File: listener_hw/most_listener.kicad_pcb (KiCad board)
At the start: 2 copper layers, 130 x 90 mm, 125 parts, among them J1 1-1394640-1, J2 ANALYSER, J3 I2S, J4 VBAT_IN, J5 PLR135/T10, J6 PLT133/T10W, J7 RCA 75R, M1 Tang Nano 20K, M2 ESP32-DevKitC-VIE, U1 74LVC1G34, U10 TPS2553DBVR, U11 74LVC1G123, U12 DIR9001, U13 SRC4192, U14 LP5907MFX-3.3, U2 74LVC1G157, U3 74LVC1G125, U4 74LVC1G123, U5 TPS7B8133DRV, U6 LMR38020F, U7 Si514, U8 LP5907MFX-3.3, U9 74LVC1G79, X1 24.576MHz

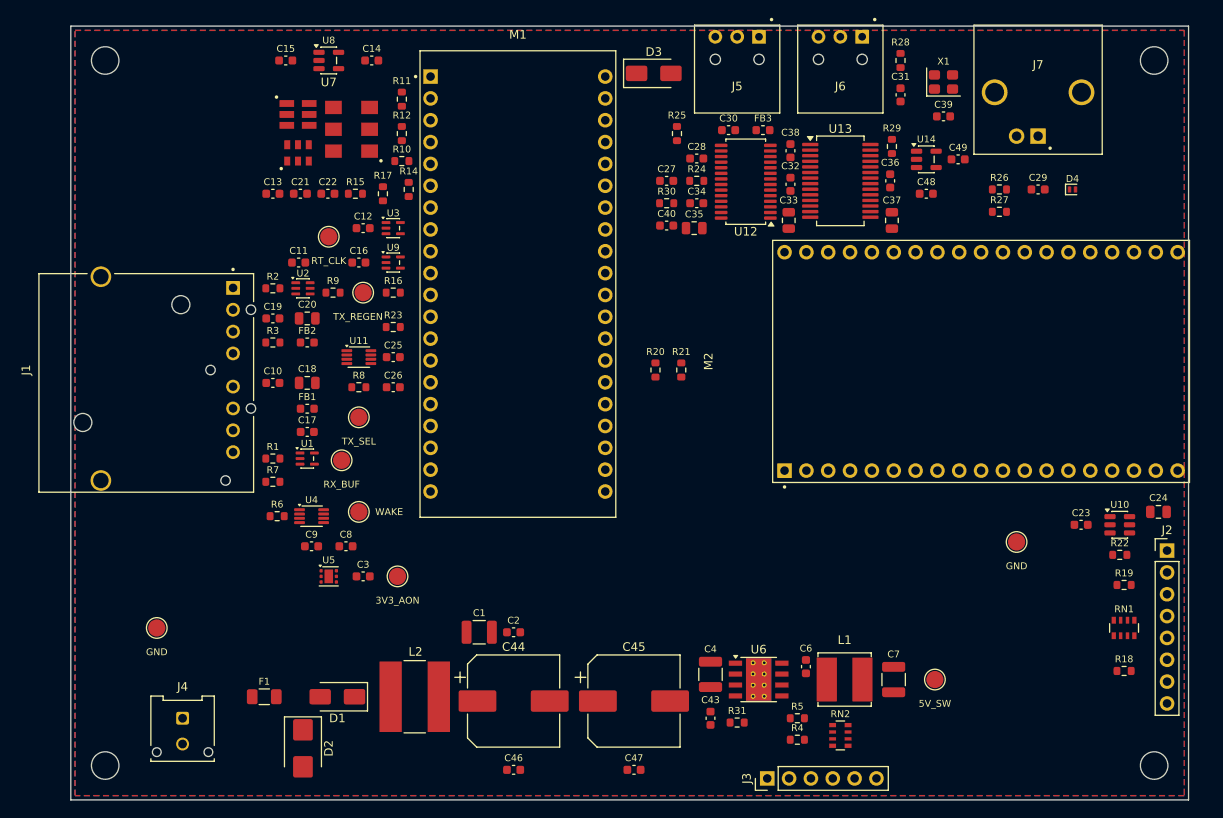
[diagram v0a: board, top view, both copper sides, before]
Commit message: Board: routed - FreeRouting session imported by the generator; J4 a right-angle Micro-Fit on the left edge; U14 in the corridor; Rail net class
most_listener.ses is FreeRouting 2.4.1's session for the exported placement
(-mp 100 -mt 1, about four minutes); gen_listener_pcb.py imports it when it
lies beside the sheet, lays the top ground pour over the tracks, fills both
pours and saves - so the routed board, too, is reproduced from the committed
files (check_all.py now diffs the .kicad_pcb and the generated .kicad_dru as
well). DRC: no error, no unconnected item; the twelve warnings are the flush
connectors' silk clipped by the board edge.

What it took: the Specctra export carries only the bottom pour. With pours
on both sides the router left GND pads on scraps of the top pour between
foreign tracks, with no room for a via (a stub-and-via stitching pass was
tried and dropped); with the bottom plane alone it escapes every GND pad to
it by a via, and the top pour laid afterwards just adds copper. The sheet's
unconnected-* nets get no net on the board (U7 has three pad-5 copies in
one such net and the router tried to join them). The 3.3 V rails moved from
Power to a Rail class of 0.35 mm - tens of milliamps, and 0.6 mm does not
pass between a module's pins. U14 (block 9's LDO) sits in the corridor under
D3, where 5V_SW arrives from below without crossing block 9; R20/R21 sit
under M2's IO25/IO27 pins; R6 and C9 at U4's right column, where the pins
they serve are. most_listener.kicad_dru asks for one resolved thermal spoke
instead of two.

J4 is now Molex Micro-Fit 3.0 43650-0200, right-angle, flush on the left
edge under J1 (mating housing 43645-0200, terminals 43030): the car's two
cables, fibre and power, leave through one face and the audio through the
top. The user asked whether the power connector could join the others on one
side; everything on the top edge would have dragged the battery input next
to the Si514 and the FOT cluster.

Co-Authored-By: Claude Fable 5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
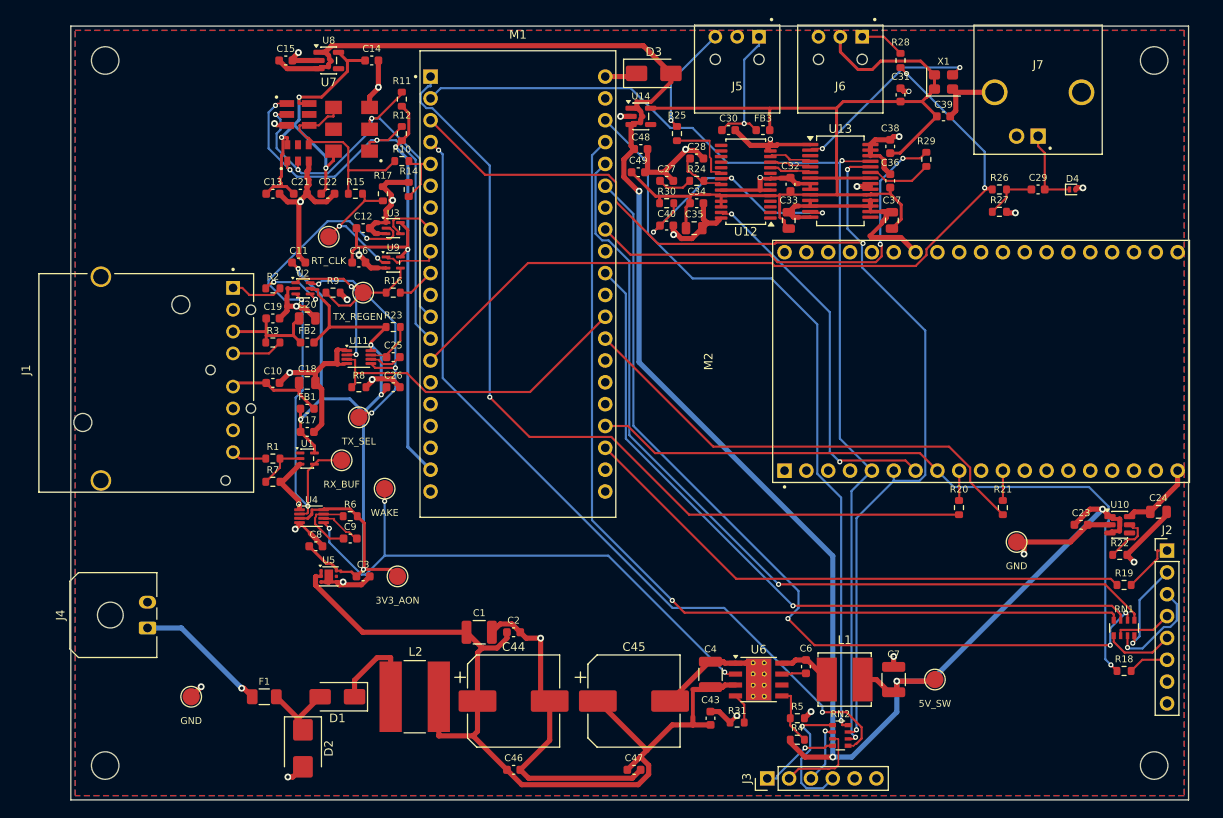
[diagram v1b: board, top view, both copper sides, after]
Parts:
- J4: footprint Molex_Micro-Fit_3.0_43045-0212_2x01_P3.00mm_Vertical -> Molex_Micro-Fit_3.0_43650-0200_1x02_P3.00mm_Horizontal
- moved R21 40.7 mm to (108.4, 56.0)
- moved R20 38.8 mm to (103.3, 56.0)
- moved C49 37.2 mm to (66.0, 17.0)
- moved C48 33.6 mm to (66.3, 14.3)
- moved U14 33.6 mm to (66.3, 10.5)
- moved C38 11.6 mm to (95.3, 14.0)
- moved J4 11.3 mm to (8.92, 70.0), turned to 90 degrees
- moved TP8 8.94 mm to (14.0, 78.0)
- moved R6 8.50 mm to (32.5, 57.0), turned to 180 degrees
- moved C9 4.59 mm to (32.5, 59.6)
- moved R29 4.27 mm to (99.5, 15.5)
- moved TP4 4.04 mm to (36.5, 53.8)
- moved C8 3.50 mm to (28.5, 60.5)
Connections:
- J1 pad 7: unconnected-(J1-STATUS-Pad7) -> (no net)
- M1 pad 11: unconnected-(M1-26_LCD_VS-Pad11) -> (no net)
- M1 pad 15: unconnected-(M1-17_LED2-Pad15) -> (no net)
- M1 pad 16: unconnected-(M1-20_LED5-Pad16) -> (no net)
- M1 pad 17: unconnected-(M1-19_LED4-Pad17) -> (no net)
- M1 pad 18: unconnected-(M1-18_LED3-Pad18) -> (no net)
- M1 pad 27: unconnected-(M1-56_I2S_BCLK-Pad27) -> (no net)
- M1 pad 29: unconnected-(M1-51_PA_EN-Pad29) -> (no net)
- M1 pad 31: unconnected-(M1-55_I2S_LRCK-Pad31) -> (no net)
- M1 pad 34: unconnected-(M1-79_WS2812-Pad34) -> (no net)
- M1 pad 36: unconnected-(M1-3V3-Pad36) -> (no net)
- M1 pad 39: unconnected-(M1-53_EDID_CLK-Pad39) -> (no net)
- M1 pad 40: unconnected-(M1-52_EDID_DAT-Pad40) -> (no net)
- M1 pad 6: unconnected-(M1-15_LED0-Pad6) -> (no net)
- M1 pad 7: unconnected-(M1-16_LED1-Pad7) -> (no net)
- M2 pad 1: unconnected-(M2-3V3-Pad1) -> (no net)
- M2 pad 10: unconnected-(M2-IO26-Pad10) -> (no net)
- M2 pad 12: unconnected-(M2-IO14-Pad12) -> (no net)
- M2 pad 13: unconnected-(M2-IO12-Pad13) -> (no net)
- M2 pad 15: unconnected-(M2-IO13-Pad15) -> (no net)
- M2 pad 16: unconnected-(M2-D2-Pad16) -> (no net)
- M2 pad 17: unconnected-(M2-D3-Pad17) -> (no net)
- M2 pad 18: unconnected-(M2-CMD-Pad18) -> (no net)
- M2 pad 2: unconnected-(M2-EN-Pad2) -> (no net)
- M2 pad 21: unconnected-(M2-IO23-Pad21) -> (no net)
- M2 pad 22: unconnected-(M2-IO22-Pad22) -> (no net)
- M2 pad 23: unconnected-(M2-TX-Pad23) -> (no net)
- M2 pad 24: unconnected-(M2-RX-Pad24) -> (no net)
- M2 pad 25: unconnected-(M2-IO21-Pad25) -> (no net)
- M2 pad 27: unconnected-(M2-IO19-Pad27) -> (no net)
- M2 pad 28: unconnected-(M2-IO18-Pad28) -> (no net)
- M2 pad 29: unconnected-(M2-IO5-Pad29) -> (no net)
- M2 pad 3: unconnected-(M2-VP-Pad3) -> (no net)
- M2 pad 30: unconnected-(M2-IO17-Pad30) -> (no net)
- M2 pad 31: unconnected-(M2-IO16-Pad31) -> (no net)
- M2 pad 32: unconnected-(M2-IO4-Pad32) -> (no net)
- M2 pad 33: unconnected-(M2-IO0-Pad33) -> (no net)
- M2 pad 34: unconnected-(M2-IO2-Pad34) -> (no net)
- M2 pad 35: unconnected-(M2-IO15-Pad35) -> (no net)
- M2 pad 36: unconnected-(M2-D1-Pad36) -> (no net)
- M2 pad 37: unconnected-(M2-D0-Pad37) -> (no net)
- M2 pad 38: unconnected-(M2-CLK-Pad38) -> (no net)
- M2 pad 4: unconnected-(M2-VN-Pad4) -> (no net)
- U1 pad 1: unconnected-(U1-NC-Pad1) -> (no net)
- U10 pad 4: unconnected-(U10-~{FAULT}-Pad4) -> (no net)
- U12 pad 1: unconnected-(U12-AUDIO-Pad1) -> (no net)
- U12 pad 15: unconnected-(U12-COUT-Pad15) -> (no net)
- U12 pad 16: unconnected-(U12-UOUT-Pad16) -> (no net)
- U12 pad 17: unconnected-(U12-EMPH-Pad17) -> (no net)
- U12 pad 18: unconnected-(U12-BFRAME-Pad18) -> (no net)
- U12 pad 2: unconnected-(U12-FSOUT0-Pad2) -> (no net)
- U12 pad 3: unconnected-(U12-FSOUT1-Pad3) -> (no net)
- U12 pad 4: unconnected-(U12-SCKO-Pad4) -> (no net)
- U12 pad 7: unconnected-(U12-XTO-Pad7) -> (no net)
- U12 pad 9: unconnected-(U12-CLKST-Pad9) -> (no net)
- U13 pad 15: unconnected-(U13-RDY-Pad15) -> (no net)
- U13 pad 3: unconnected-(U13-NC-Pad3) -> (no net)
- U14 pad 4: unconnected-(U14-NC-Pad4) -> (no net)
- U5 pad 5: unconnected-(U5-NC-Pad5) -> (no net)
- U6 pad 6: unconnected-(U6-PG-Pad6) -> (no net)
- U7 pad 5: unconnected-(U7-CLK--Pad5) -> (no net)
- U8 pad 4: unconnected-(U8-NC-Pad4) -> (no net)
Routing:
- net GND: track 0.00 -> 282.2 mm, vias 0 -> 31
- net 5V_SW: track 0.00 -> 216.7 mm, vias 0 -> 4
- net /I2S_LRCK_F: track 0.00 -> 136.8 mm, vias 0 -> 3
- net 3V3_DA: track 0.00 -> 127.7 mm
- net /I2S_BCLK_F: track 0.00 -> 125.9 mm, vias 0 -> 2
- net /SD1_F: track 0.00 -> 110.5 mm, vias 0 -> 1
- net 3V3_AON: track 0.00 -> 106.1 mm, vias 0 -> 5
- net /FS_F: track 0.00 -> 104.4 mm, vias 0 -> 3
- net VBAT_P: track 0.00 -> 102.8 mm
- net /BCLK_F: track 0.00 -> 102.2 mm, vias 0 -> 1
- net /UART_RX_F: track 0.00 -> 101.9 mm, vias 0 -> 1
- net /I2S_MCLK_F: track 0.00 -> 97.2 mm, vias 0 -> 2
- net /SPDIF_F: track 0.00 -> 93.3 mm, vias 0 -> 2
- net /I2S_DOUT_F: track 0.00 -> 87.8 mm, vias 0 -> 1
- net /SD0_F: track 0.00 -> 86.9 mm, vias 0 -> 1
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
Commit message: Board: copper removed - routed by hand in KiCad from here; the generator only lays out (--fresh) and never overwrites the board
The FreeRouting result is gone: the battery path hopped layers for no
reason, the electrolytics' ground pads looped through the 100 nF caps instead
of dropping into the pour, and the rest was of the same kind. An autorouter
does not make the decisions a power block, a clock line or a receiver front
end need; from here the board is routed by hand in the PCB editor.

most_listener.kicad_pcb is therefore the master file: parts may be moved
freely, and gen_listener_pcb.py refuses to overwrite it unless run with
--fresh, which lays the parts out again from PLACE and discards every track.
The board it wrote now carries the placement, the outline, the holes, both
ground pours, the antenna keep-out, the net classes (Default 0.25/0.15, Rail
0.35, Power 0.6 mm) and the DRC rules file, and no tracks. Sheet changes reach
the board through Update PCB from Schematic. The Specctra export, the session
import and the stray-via clean-up are removed from the generator;
most_listener.ses is deleted. check_all.py runs the board's DRC only (errors
from the JSON report, since the exit code would count the unconnected items)
and no longer diffs the board or the project file. README: The board.

Co-Authored-By: Claude Fable 5.1 <noreply@anthropic.com>
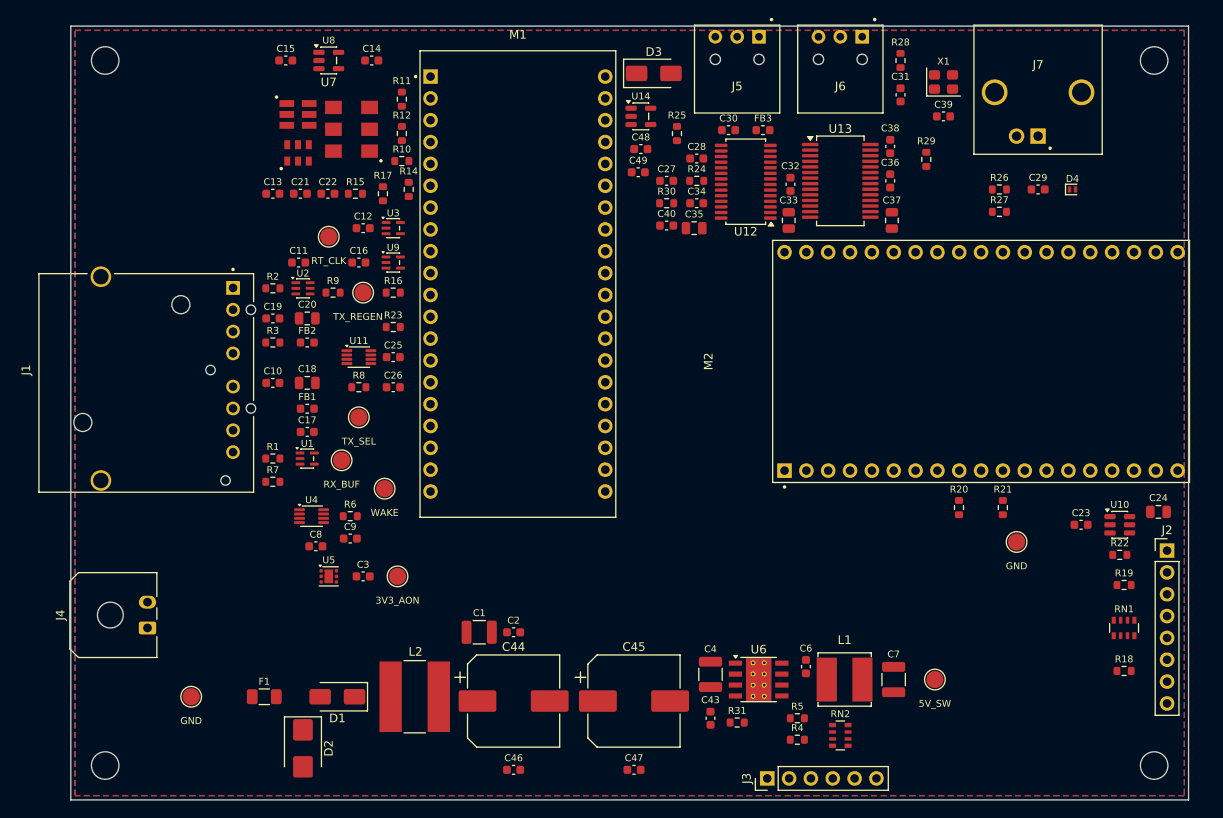
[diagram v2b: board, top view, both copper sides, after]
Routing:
- net GND: track 282.2 -> 0.00 mm, vias 31 -> 0
- net 5V_SW: track 216.7 -> 0.00 mm, vias 4 -> 0
- net /I2S_LRCK_F: track 136.8 -> 0.00 mm, vias 3 -> 0
- net 3V3_DA: track 127.7 -> 0.00 mm
- net /I2S_BCLK_F: track 125.9 -> 0.00 mm, vias 2 -> 0
- net /SD1_F: track 110.5 -> 0.00 mm, vias 1 -> 0
- net 3V3_AON: track 106.1 -> 0.00 mm, vias 5 -> 0
- net /FS_F: track 104.4 -> 0.00 mm, vias 3 -> 0
- net VBAT_P: track 102.8 -> 0.00 mm
- net /BCLK_F: track 102.2 -> 0.00 mm, vias 1 -> 0
- net /UART_RX_F: track 101.9 -> 0.00 mm, vias 1 -> 0
- net /I2S_MCLK_F: track 97.2 -> 0.00 mm, vias 2 -> 0
- net /SPDIF_F: track 93.3 -> 0.00 mm, vias 2 -> 0
- net /I2S_DOUT_F: track 87.8 -> 0.00 mm, vias 1 -> 0
- net /SD0_F: track 86.9 -> 0.00 mm, vias 1 -> 0
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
